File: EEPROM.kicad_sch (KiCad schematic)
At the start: 2 parts, among them U701 24LC256

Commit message: added something to debug the channel buttons
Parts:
- C701: footprint Capacitor_THT:C_Disc_D3.0mm_W1.6mm_P2.50mm -> Capacitor_SMD:C_0805_2012Metric
- U701: footprint Package_DIP:DIP-8_W7.62mm_Socket -> Package_SO:SOIC-8_3.9x4.9mm_P1.27mm
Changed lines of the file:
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@@
       (effects (font (size 1.27 1.27)) (justify left))
     )
-    (property "Footprint" "Capacitor_THT:C_Disc_D3.0mm_W1.6mm_P2.50mm" (id 2) (at 119.0752 87.63 0)
+    (property "Footprint" "Capacitor_SMD:C_0805_2012Metric" (id 2) (at 119.0752 87.63 0)
       (effects (font (size 1.27 1.27)) hide)
     )
@@
       (effects (font (size 1.27 1.27)) (justify left))
     )
-    (property "Footprint" "Package_DIP:DIP-8_W7.62mm_Socket" (id 2) (at 139.7 86.36 0)
+    (property "Footprint" "Package_SO:SOIC-8_3.9x4.9mm_P1.27mm" (id 2) (at 139.7 86.36 0)
       (effects (font (size 1.27 1.27)) hide)
     )

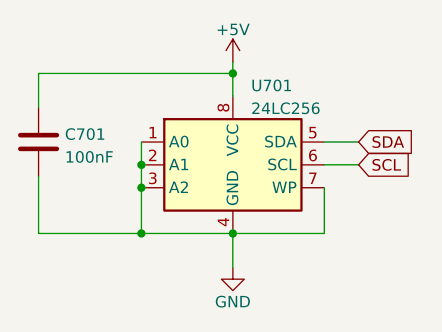
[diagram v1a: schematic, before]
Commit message: redid this project. I want to use an atmega328 so I ditched some IO. I retained 4 servo, 1 H-bridge (should make it double), 3 relays, 6 GPIO, 1 potentiometer and loconet interface. And I still have a config button
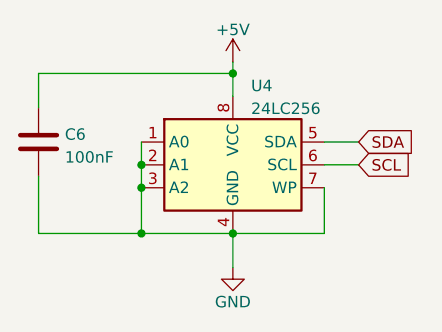
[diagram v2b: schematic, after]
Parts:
- renumbered C701 to C6, U701 to U4
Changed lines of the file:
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@@
   (symbol (lib_id "Device:C") (at 118.11 83.82 0) (unit 1)
     (in_bom yes) (on_board yes) (fields_autoplaced)
-    (property "Reference" "C701" (id 0) (at 121.031 82.9853 0)
+    (property "Reference" "C6" (id 0) (at 121.031 82.9853 0)
       (effects (font (size 1.27 1.27)) (justify left))
     )
@@
   (symbol (lib_id "Memory_EEPROM:24LC256") (at 139.7 86.36 0) (unit 1)
     (in_bom yes) (on_board yes) (fields_autoplaced)
-    (property "Reference" "U701" (id 0) (at 141.7194 77.5802 0)
+    (property "Reference" "U4" (id 0) (at 141.7194 77.5802 0)
       (effects (font (size 1.27 1.27)) (justify left))
     )
@@
   (symbol (lib_id "power:+5V") (at 139.7 74.93 0) (unit 1)
     (in_bom yes) (on_board yes) (fields_autoplaced)
-    (property "Reference" "#PWR0701" (id 0) (at 139.7 78.74 0)
+    (property "Reference" "#PWR021" (id 0) (at 139.7 78.74 0)
       (effects (font (size 1.27 1.27)) hide)
     )
@@
   (symbol (lib_id "power:GND") (at 139.7 97.79 0) (unit 1)
     (in_bom yes) (on_board yes)
-    (property "Reference" "#PWR0702" (id 0) (at 139.7 104.14 0)
+    (property "Reference" "#PWR022" (id 0) (at 139.7 104.14 0)
       (effects (font (size 1.27 1.27)) hide)
     )
